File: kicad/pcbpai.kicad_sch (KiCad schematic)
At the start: 15 parts, among them J1 Fusible, J2 Conn_01x04_Pin, J3 Input 24 V, J4 Boton Encendido, J5 Parada de Emergencia, J6 Conn_01x06_Pin, J8 Conn_01x09_Pin, SW1 SW_Push_DPDT, U6 ATtiny85-20P

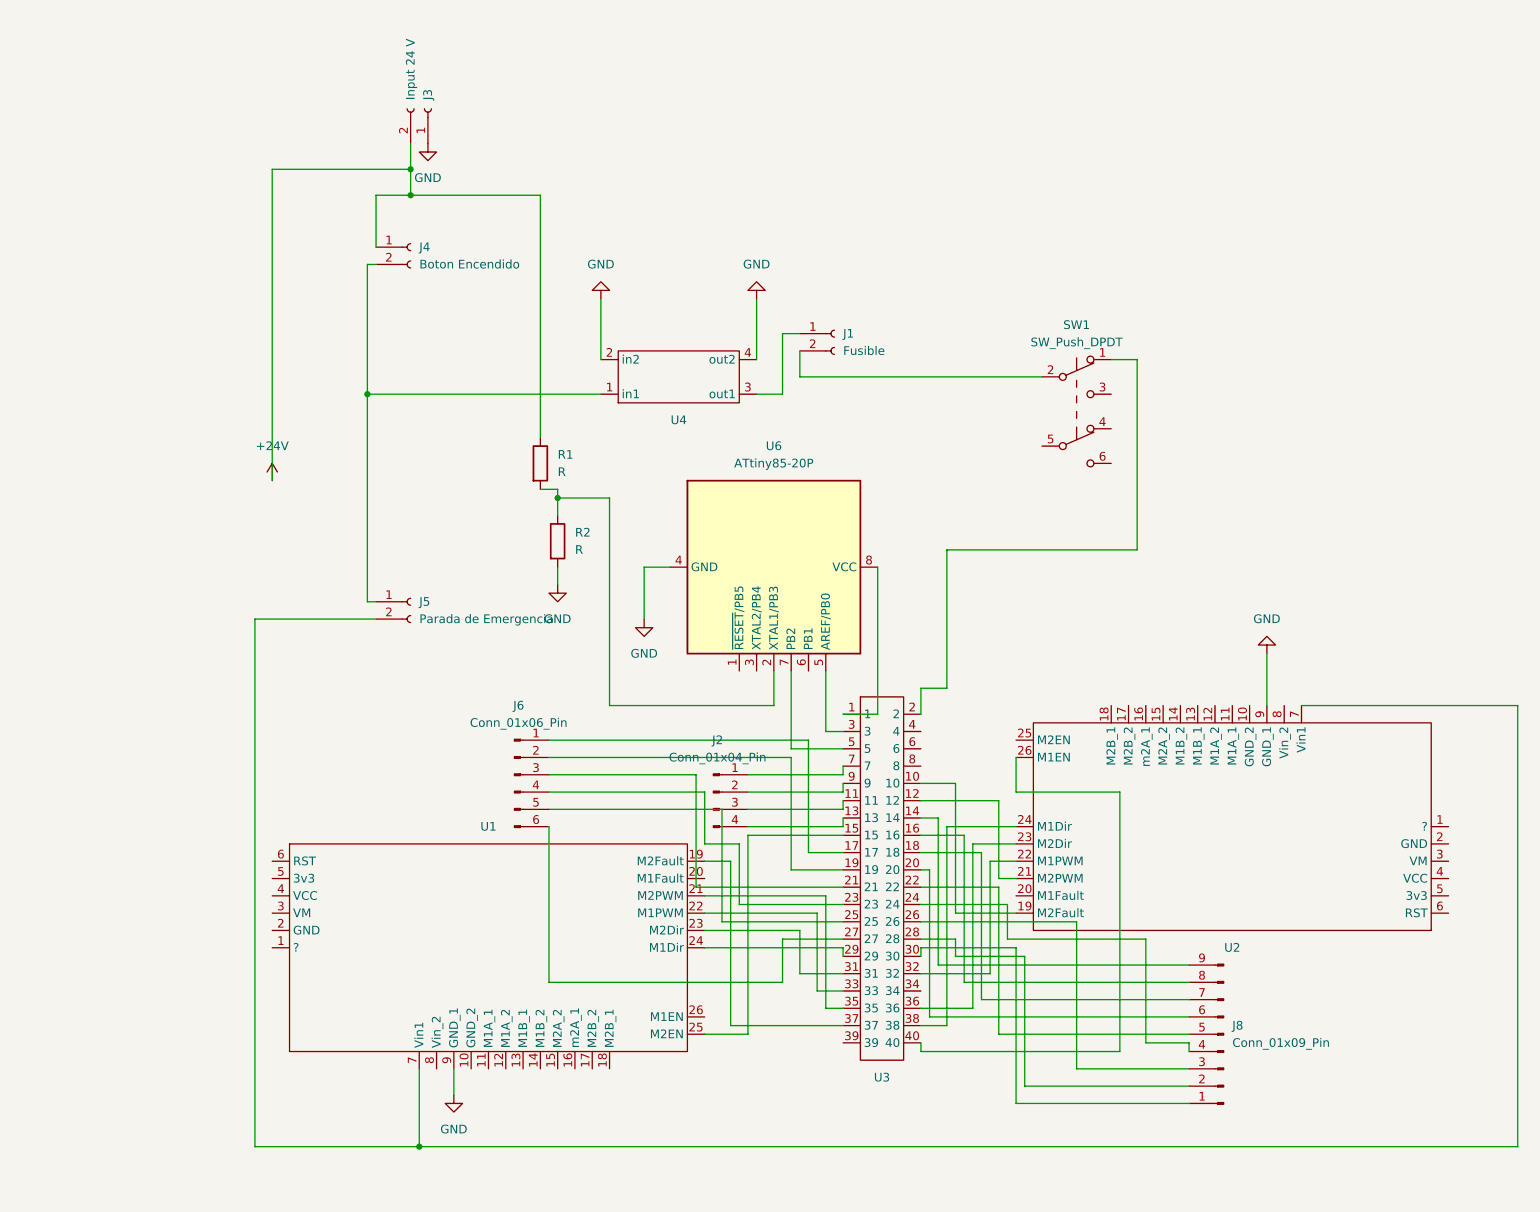
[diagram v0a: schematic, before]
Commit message: add 3d models and footprints to kicad
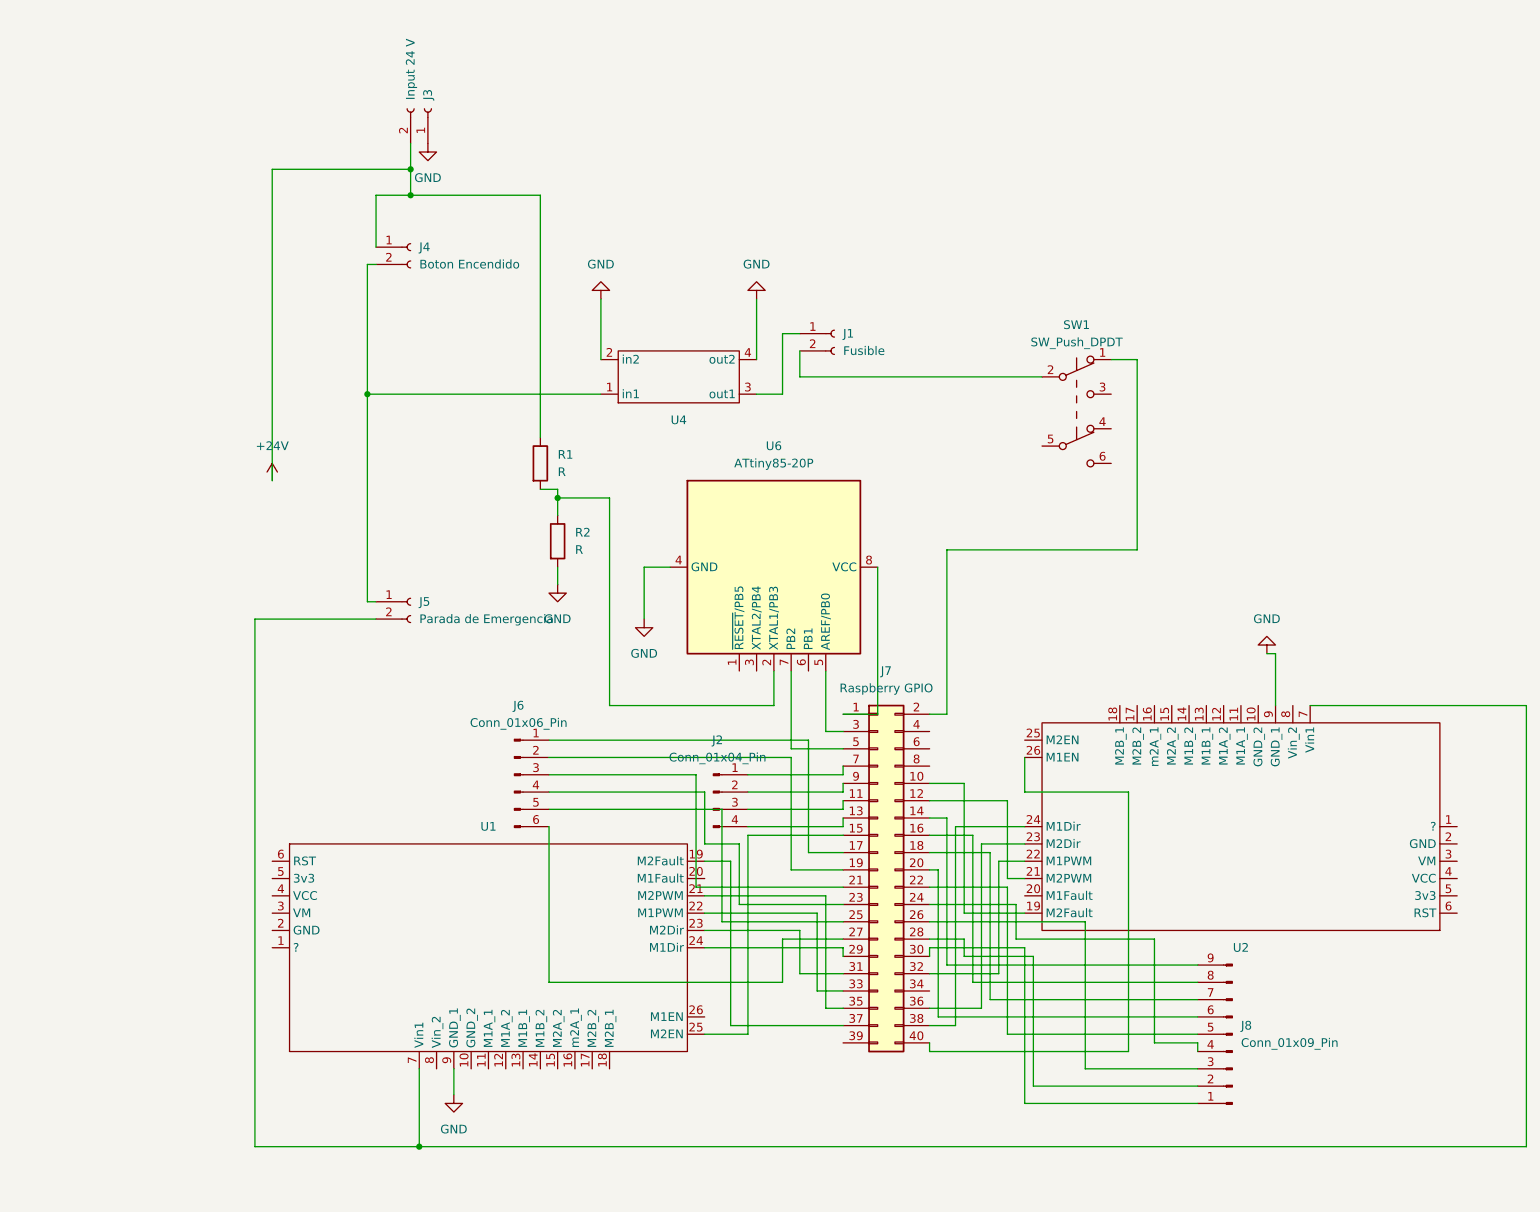
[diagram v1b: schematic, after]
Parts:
- removed U3: ~, libpai:raspberry, symbol LibPai:Raspberry
- added J7: Raspberry GPIO, Connector_PinHeader_2.54mm:PinHeader_2x20_P2.54mm_Vertical, symbol Connector_Generic:Conn_02x20_Odd_Even
- J2: footprint Connector_PinHeader_2.54mm:PinHeader_1x04_P2.54mm_Vertical -> Connector_PinSocket_2.54mm:PinSocket_1x04_P2.54mm_Vertical
- J3, J4, J5: footprint TerminalBlock_Altech:Altech_AK300_1x02_P5.00mm_45-Degree -> Connector_Phoenix_MSTB:PhoenixContact_MSTBA_2,5_2-G_1x02_P5.00mm_Horizontal
- J8: footprint Connector_PinHeader_2.54mm:PinHeader_1x09_P2.54mm_Vertical -> Connector_PinSocket_2.54mm:PinSocket_1x09_P2.54mm_Vertical
- SW1: footprint libpai:pulsador -> PAI:pulsador
- U1, U2: footprint libpai:Pololu MAX 14870 Dual Shield Arduino -> PAI:Pololu MAX 14870 Dual Shield Arduino
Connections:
- net at U1.19 (M2Fault): now also J7.37 (Pin_37)
- net at U1.21 (M2PWM): now also J7.35 (Pin_35)
- net at U1.22 (M1PWM): now also J7.33 (Pin_33)
- net at U1.23 (M2Dir): now also J7.31 (Pin_31)
- net at U1.24 (M1Dir): now also J7.29 (Pin_29)
- net at U1.25 (M2EN): now also J7.15 (Pin_15)
- net at SW1.1 (A): now also J7.2 (Pin_2)
- net at U2.19 (M2Fault): now also J7.10 (Pin_10)
- net at U2.21 (M2PWM): now also J7.12 (Pin_12)
- net at U2.22 (M1PWM): now also J7.32 (Pin_32)
- net at U2.23 (M2Dir): now also J7.36 (Pin_36)
- net at U2.24 (M1Dir): now also J7.38 (Pin_38)
- net at U2.26 (M1EN): now also J7.40 (Pin_40)
- net at U6.8 (VCC): now also J7.1 (Pin_1)
- net at J2.3 (Pin_3): now also J7.11 (Pin_11)
- net at J2.4 (Pin_4): now also J7.13 (Pin_13)
- net at J8.9 (Pin_9): now also J7.14 (Pin_14)
- net at J8.8 (Pin_8): now also J7.16 (Pin_16)
- net at J6.1 (Pin_1): now also J7.17 (Pin_17)
- net at J8.7 (Pin_7): now also J7.18 (Pin_18)
- net at J6.2 (Pin_2): now also J7.19 (Pin_19)
- net at J8.6 (Pin_6): now also J7.20 (Pin_20)
- net at J6.3 (Pin_3): now also J7.21 (Pin_21)
- net at J8.5 (Pin_5): now also J7.22 (Pin_22)
- net at J6.4 (Pin_4): now also J7.23 (Pin_23)
- net at J8.4 (Pin_4): now also J7.24 (Pin_24)
- net at J6.5 (Pin_5): now also J7.25 (Pin_25)
- net at J8.3 (Pin_3): now also J7.26 (Pin_26)
- net at J6.6 (Pin_6): now also J7.27 (Pin_27)
- net at J8.2 (Pin_2): now also J7.28 (Pin_28)
- net at U6.5 (AREF/PB0): now also J7.3 (Pin_3)
- net at J8.1 (Pin_1): now also J7.30 (Pin_30)
- net at U6.7 (PB2): now also J7.5 (Pin_5)
- net at J2.1 (Pin_1): now also J7.7 (Pin_7)
- net at J2.2 (Pin_2): now also J7.9 (Pin_9)
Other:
- company: (none) -> Universidad Nacional de Colombia
- title: (none) -> Distribuition board
- moved on the sheet: J8, U2

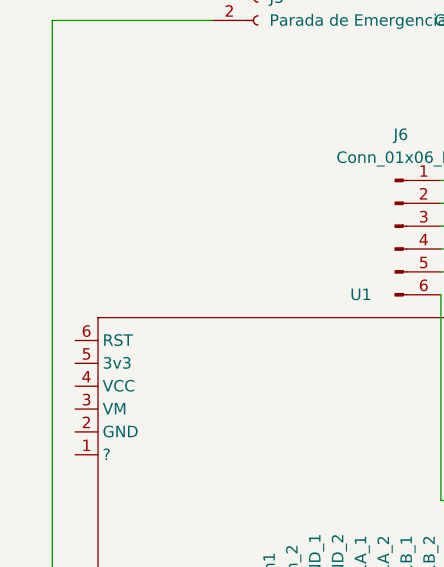
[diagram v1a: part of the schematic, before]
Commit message: center raspberry mounting holes
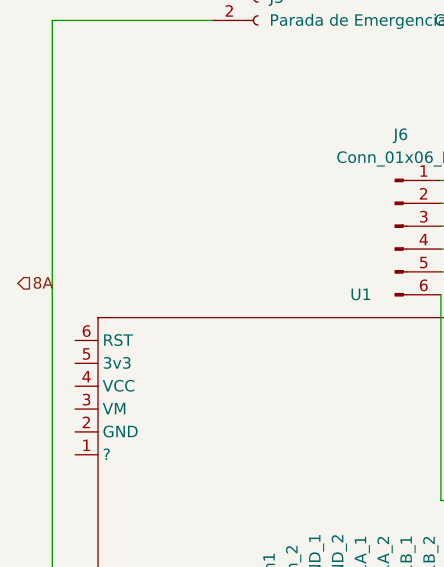
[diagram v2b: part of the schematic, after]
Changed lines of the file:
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@@
     (stroke (width 0) (type default))
+  )
+  (hierarchical_label "8A" (shape input) (at 57.15 109.22 0) (fields_autoplaced)
+    (effects (font (size 1.27 1.27)) (justify left))
+  )
+  (netclass_flag "" (length 2.54) (shape round) (at 190.5 53.34 270) (fields_autoplaced)
+    (effects (font (size 1.27 1.27)) (justify right bottom))
+    (property "Netclass" "3A" (at 193.04 52.6415 90)
+      (effects (font (size 1.27 1.27) italic) (justify left))
+    )
+  )
+  (netclass_flag "" (length 2.54) (shape round) (at 166.37 44.45 0) (fields_autoplaced)
+    (effects (font (size 1.27 1.27)) (justify left bottom))
+    (property "Netclass" "3A" (at 167.0685 41.91 0)
+      (effects (font (size 1.27 1.27) italic) (justify left))
+    )
+  )
+  (netclass_flag "" (length 2.54) (shape round) (at 138.43 43.18 90) (fields_autoplaced)
+    (effects (font (size 1.27 1.27)) (justify left bottom))
+    (property "Netclass" "3A" (at 135.89 42.4815 90)
+      (effects (font (size 1.27 1.27) italic) (justify left))
+    )
+  )
+  (netclass_flag "" (length 2.54) (shape round) (at 67.31 80.01 0) (fields_autoplaced)
+    (effects (font (size 1.27 1.27)) (justify left bottom))
+    (property "Netclass" "3A" (at 68.0085 77.47 0)
+      (effects (font (size 1.27 1.27) italic) (justify left))
+    )
+  )
+  (netclass_flag "" (length 2.54) (shape round) (at 88.9 46.99 0) (fields_autoplaced)
+    (effects (font (size 1.27 1.27)) (justify left bottom))
+    (property "Netclass" "8A" (at 89.5985 44.45 0)
+      (effects (font (size 1.27 1.27) italic) (justify left))
+    )
   )
   (symbol (lib_id "Connector:Conn_01x02_Socket") (at 83.82 77.47 0) (unit 1)

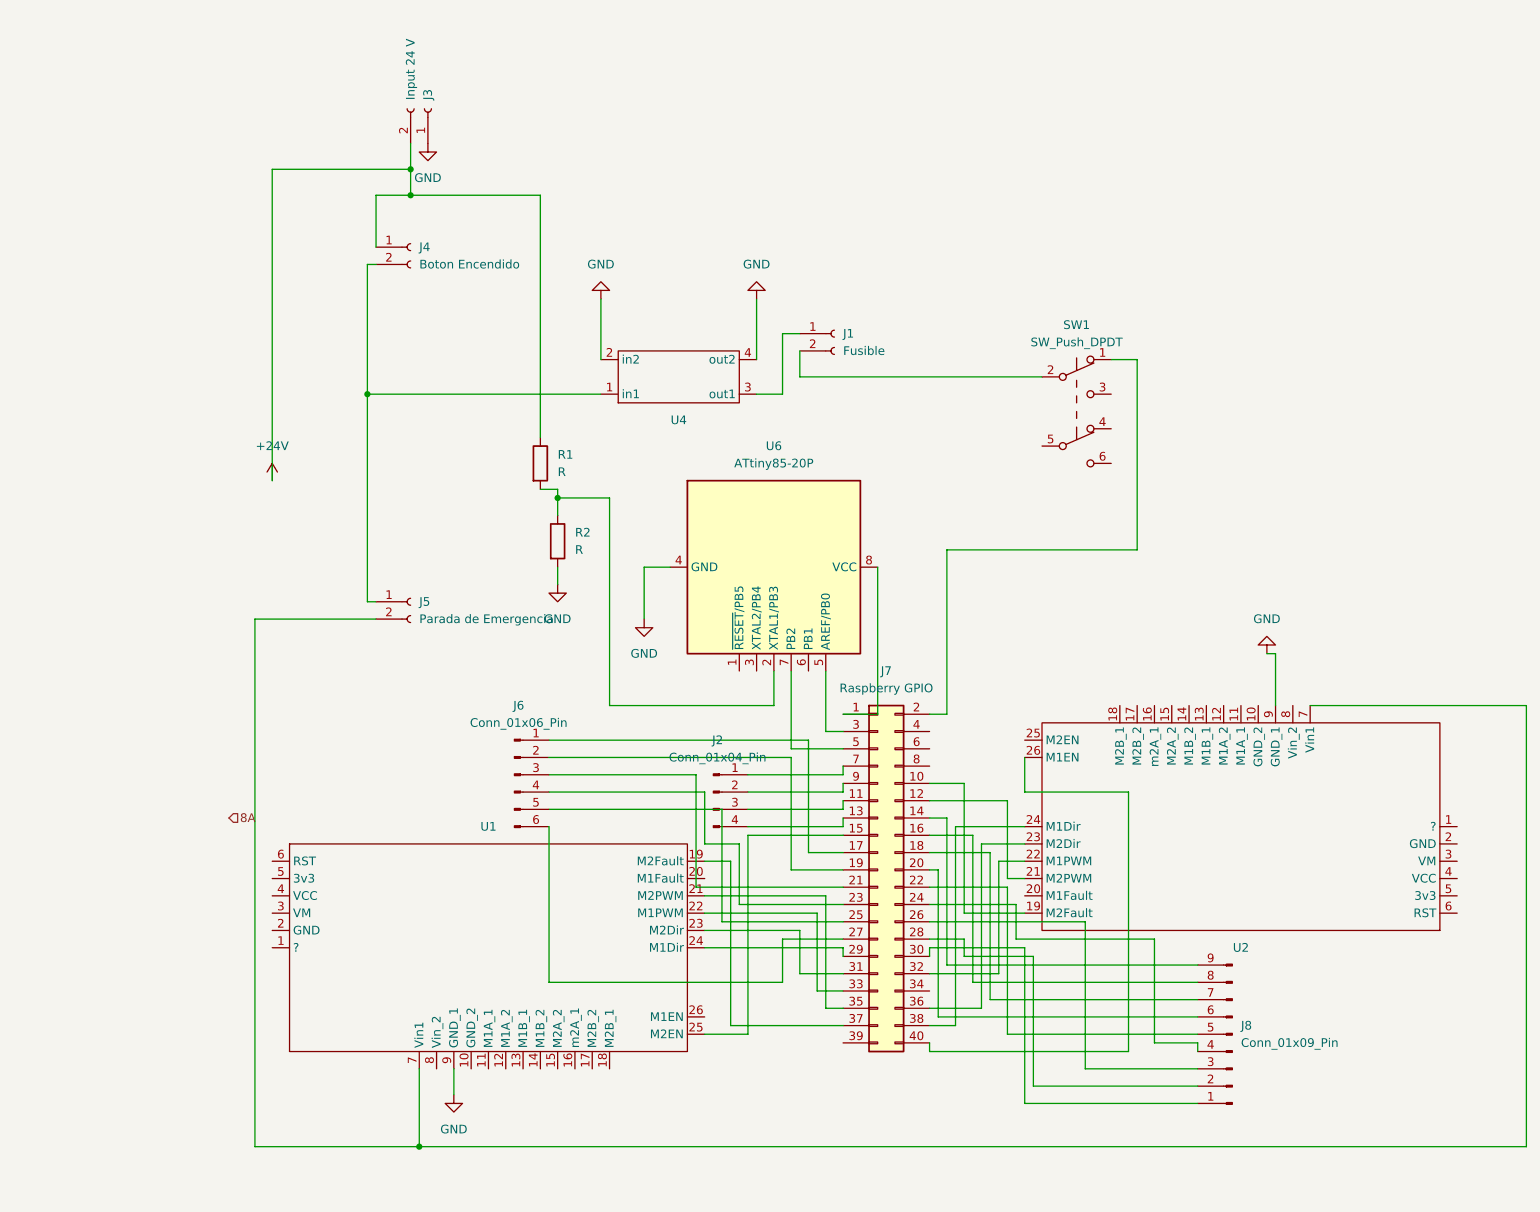
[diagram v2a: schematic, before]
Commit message: update libraries and change trace width
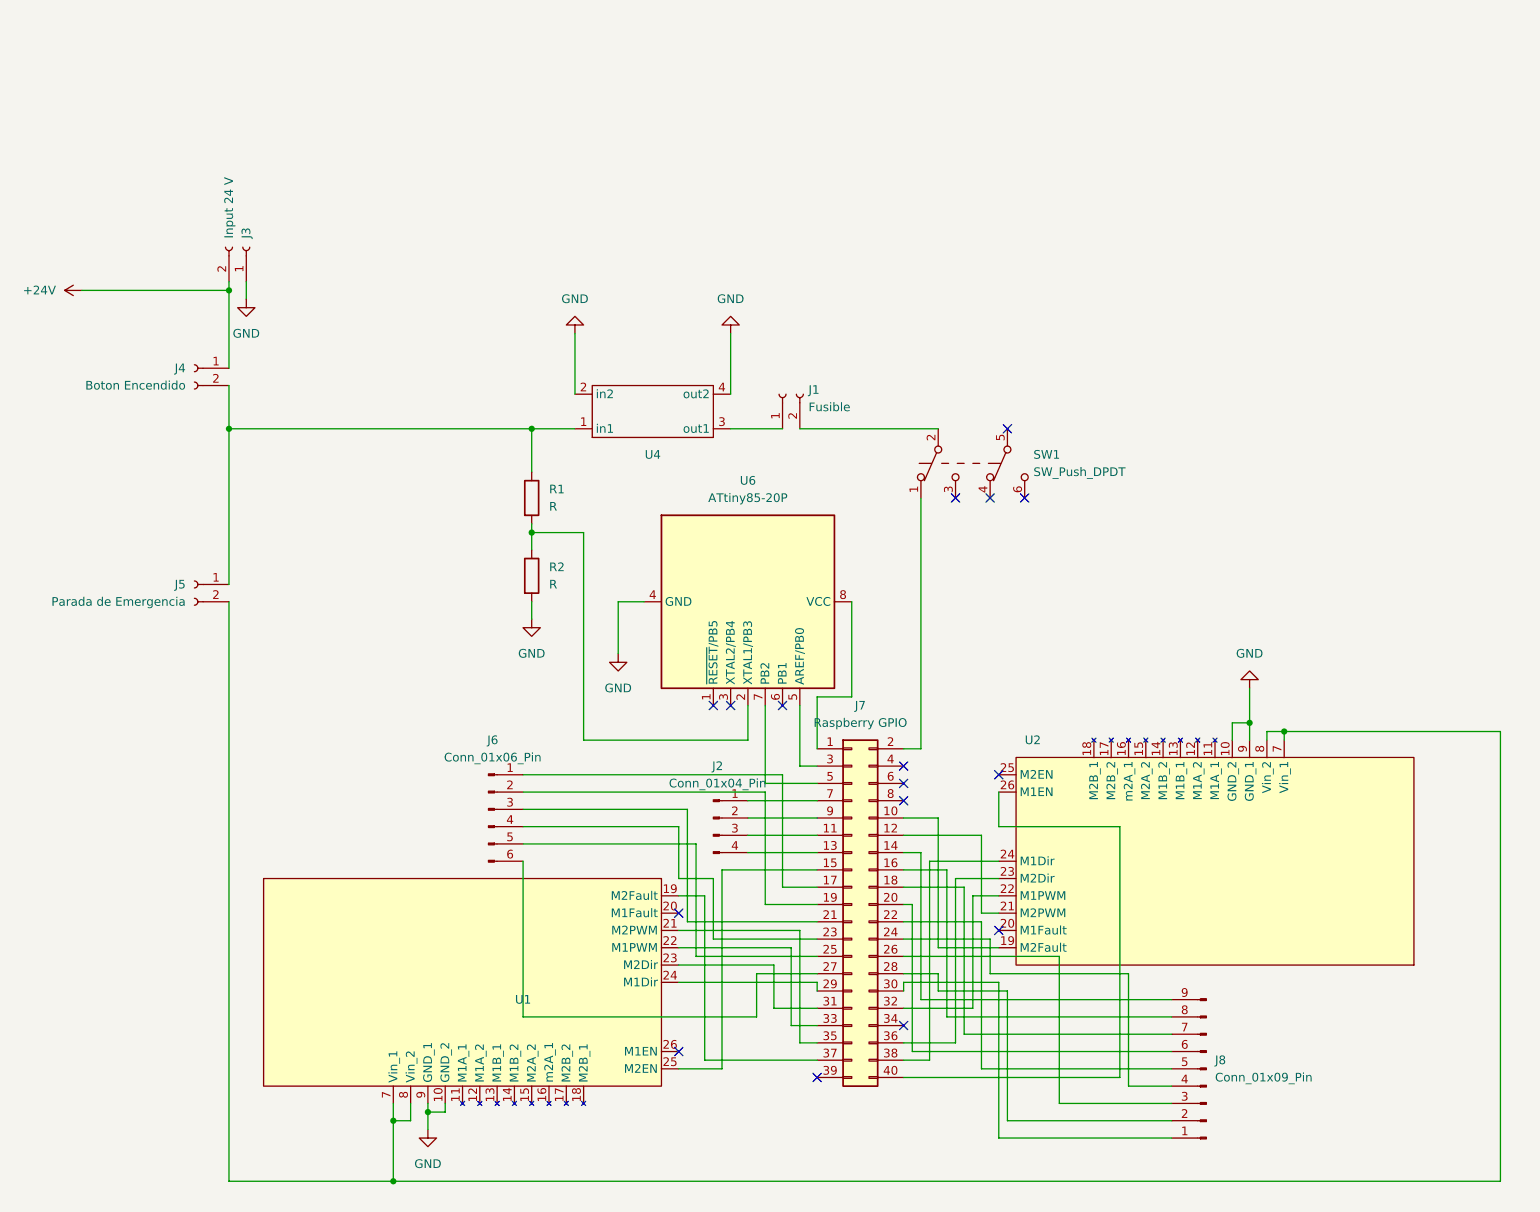
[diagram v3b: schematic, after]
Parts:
- J1: footprint libpai:fusible -> PAI:fusible
- J3: footprint Connector_Phoenix_MSTB:PhoenixContact_MSTBA_2,5_2-G_1x02_P5.00mm_Horizontal -> Connector_AMASS:AMASS_XT60-M_1x02_P7.20mm_Vertical
- SW1: footprint PAI:pulsador -> PAI:switch
- U1, U2: symbol LibPai:Dual_MAx14870 -> Lib_PAI:Dual_MAX14870
- U4: footprint libpai:regulador -> PAI:regulador; symbol LibPai:Regulador -> Lib_PAI:Regulador
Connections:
- net +24V: no longer R1.1
- net GND: now also U1.10 (GND_2), U2.10 (GND_2)
- net at J4.2 (Pin_2), J5.1 (Pin_1), U4.1 (in1): now also R1.1
- net at J5.2 (Pin_2), U1.7 (Vin_1), U2.7 (Vin_1): now also U1.8 (Vin_2), U2.8 (Vin_2)
- no-connect marks 0 -> 16
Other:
- moved on the sheet: J1, J2, J3, J4, J5, J6, J7, J8, R1, R2, SW1, U4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
